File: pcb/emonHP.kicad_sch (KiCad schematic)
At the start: 66 parts, among them CN1 CONN_03SCREW, CN3 Screw_Terminal_01x02, CN4 CONN_03SCREW, CN5 Screw_Terminal_01x02, J2 CONN_04PTH, J3 USB_C_Receptacle_USB2.0, J4 Conn_ARM_JTAG_SWD_10, J5 Conn_02x20_Odd_Even, SW1 SW_Push, SW2 SW_Push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

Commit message: Manufactured board
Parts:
- removed U10: SN74LVC1T45DRL, Package_TO_SOT_SMD:SOT-563, symbol Logic_LevelTranslator:SN74LVC1T45DRL
- added C16: 100n, Capacitor_SMD:C_0402_1005Metric, symbol Device:C
- added J1: Conn_01x02, Connector_PinHeader_2.54mm:PinHeader_1x02_P2.54mm_Vertical, symbol Connector_Generic:Conn_01x02
- added R21, R24, R25, R3: 10K, Resistor_SMD:R_0402_1005Metric, symbol Device:R
- C12: LCSC (none) -> C52923
- C7: LCSC C1525 -> C23630
- D2, D3, D4: LCSC (none) -> C22440024
- FB1, FB2: LCSC (none) -> C237347
- J3: LCSC C27636760 -> C2765186
- J4: LCSC (none) -> C150517; now fitted
- LED1: LCSC (none) -> C125116
- R1: value 4K7 -> 5K1
- R11, R7: LCSC (none) -> C25744
- SW2: LCSC (none) -> C2689642
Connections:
- net +3V3: now also C16.1, R24.1; no longer D10.2 (A)
- net Boost/36V: now also J1.1 (Pin_1)
- net GND: now also C16.2, J1.2 (Pin_2), R21.2, R25.2
- net MBUS_OC: now also U2.9 (PA04)
- net RS485_RX5: now also R3.1
- net UART3_RTS: now also R25.1
- net UART3_RX: now also R21.1, R3.2
- net UART3_TX: now also R24.2
- net Vuc: now also D10.2 (A)
- net ~{LED_ACT}: now also U2.37 (PB22); no longer U2.9 (PA04)
- no-connect marks 25 -> 28
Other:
- moved on the sheet: CN5

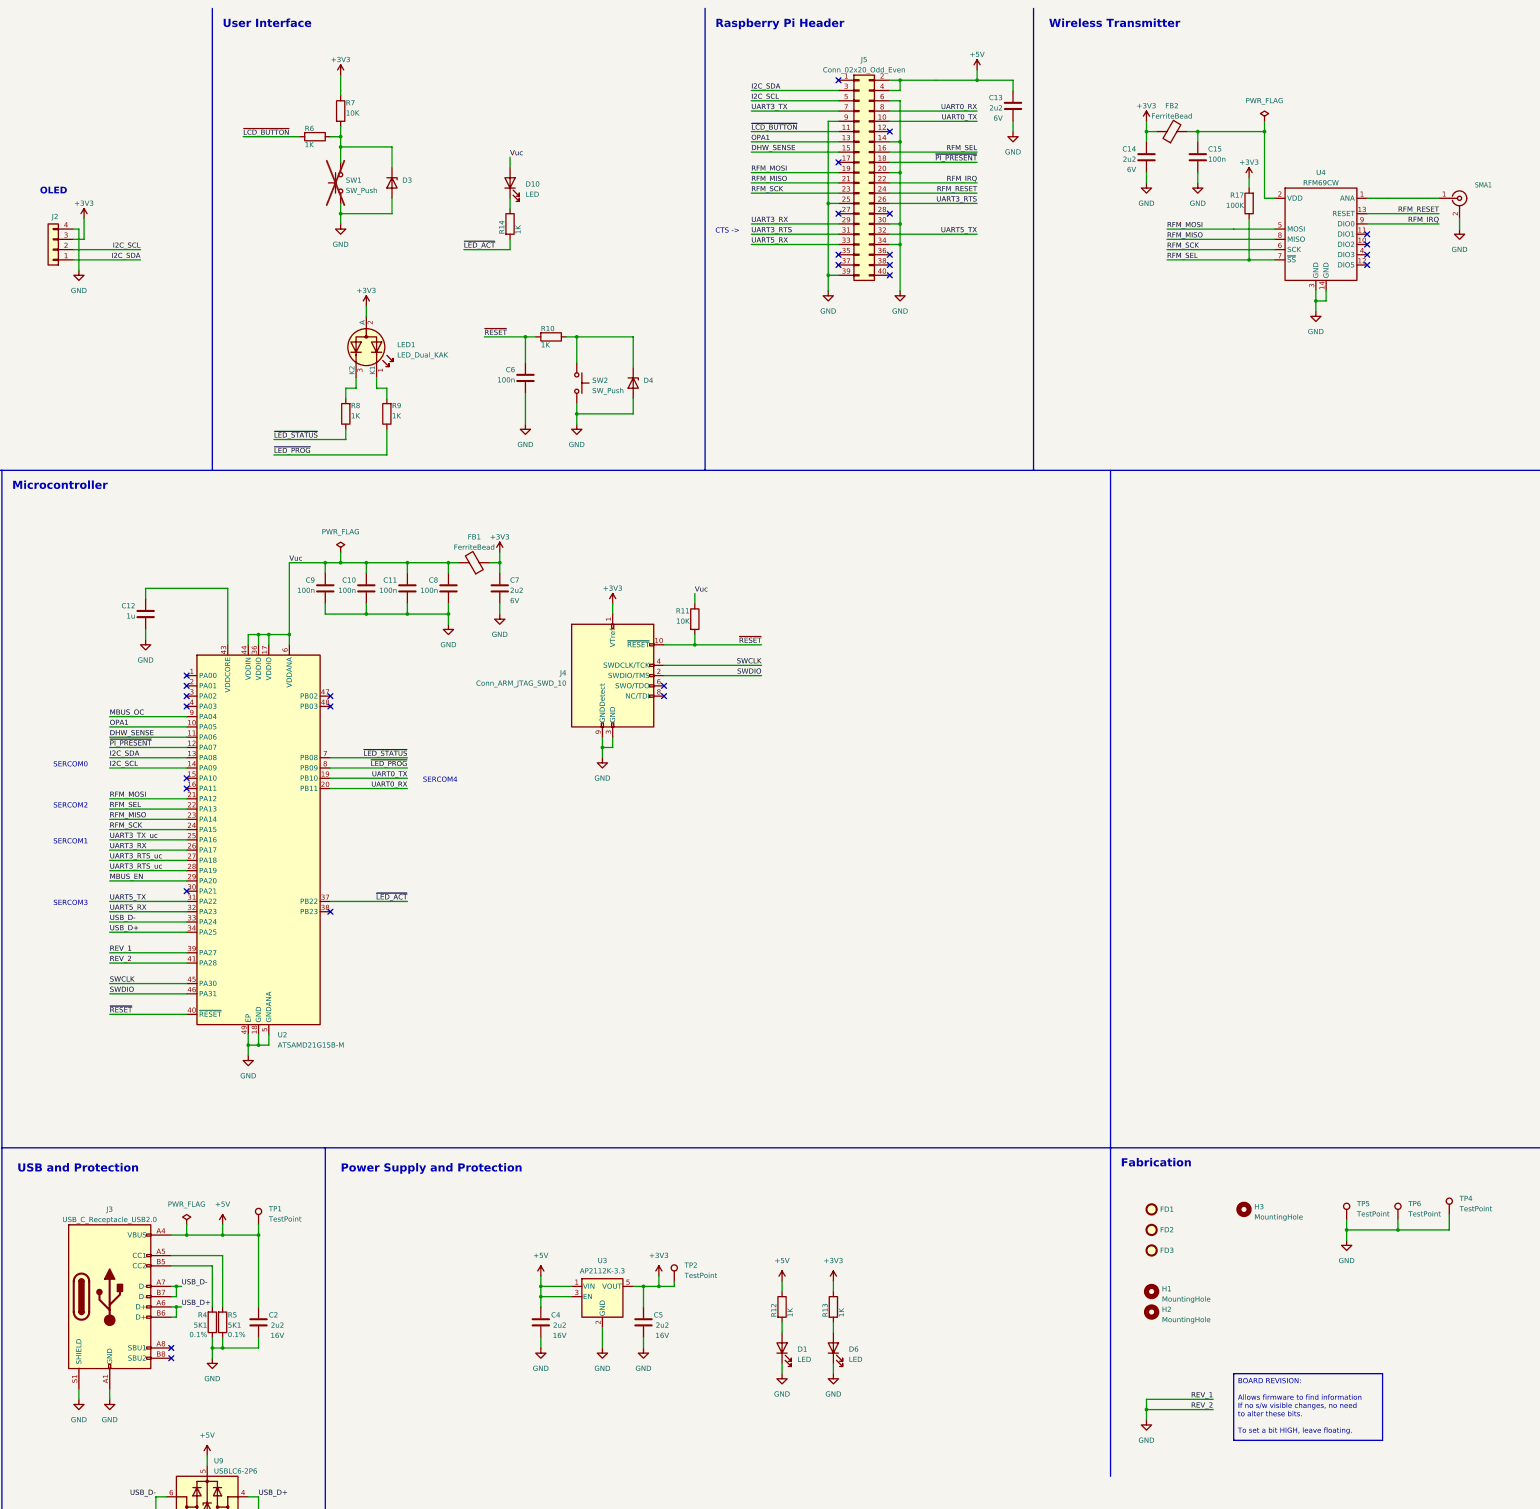
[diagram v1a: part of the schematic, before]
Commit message: emonHP with Pi attachment
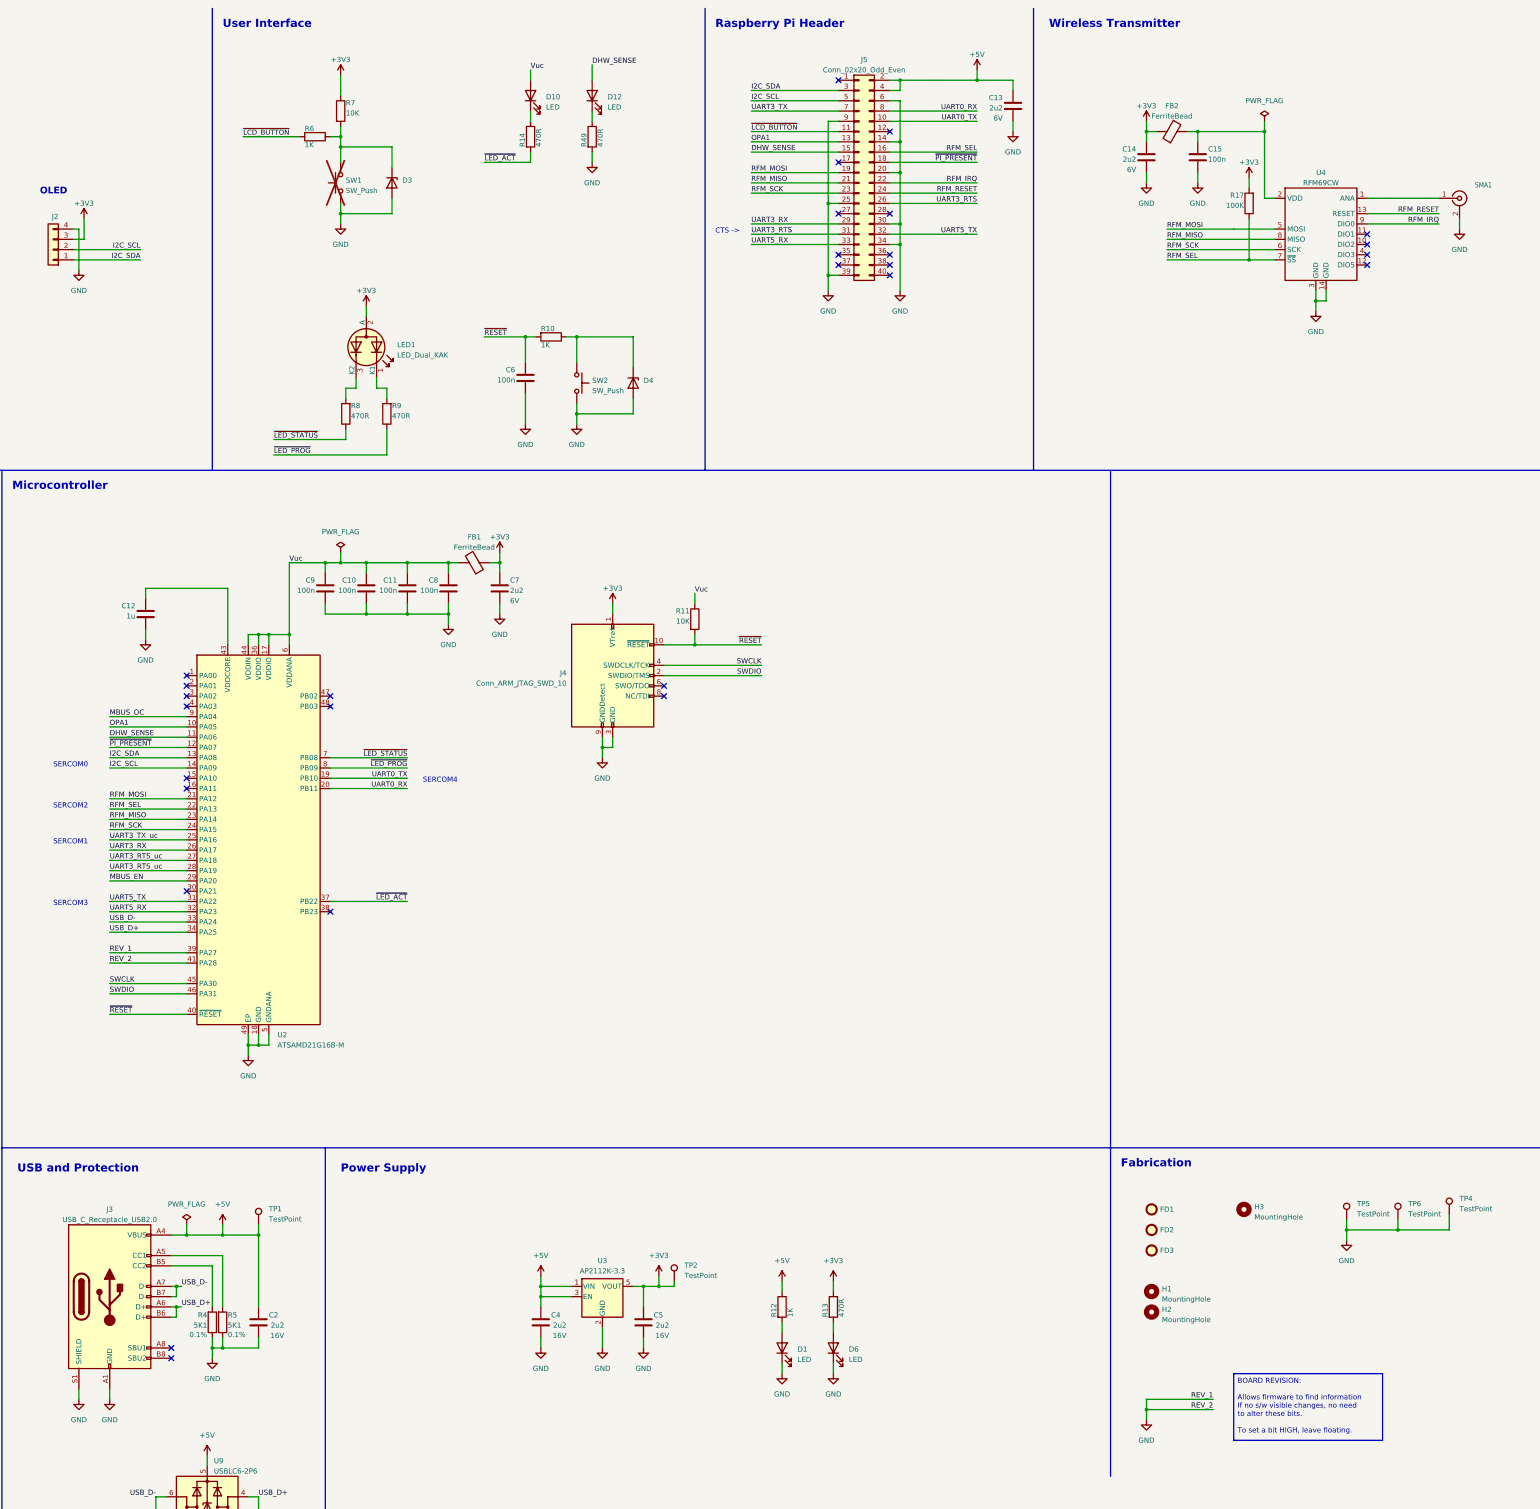
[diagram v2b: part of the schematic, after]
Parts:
- removed U2: ATSAMD21G15B-M, Package_DFN_QFN:QFN-48-1EP_7x7mm_P0.5mm_EP5.15x5.15mm, symbol MCU_Microchip_SAMD:ATSAMD21G15B-M
- added D12: LED, LED_SMD:LED_0603_1608Metric, symbol Device:LED
- added R49: 470R, Resistor_SMD:R_0402_1005Metric, symbol Device:R
- added U2: ATSAMD21G16B-M, Package_DFN_QFN:QFN-48-1EP_7x7mm_P0.5mm_EP5.15x5.15mm, symbol MCU_Microchip_SAMD:ATSAMD21G16B-M
- R13, R14, R8, R9: value 1K -> 470R; LCSC C11702 -> C25117
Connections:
- net DHW_SENSE: now also D12.2 (A), U2.11 (PA06)
- net GND: now also R49.2, U2.18 (GND), U2.35 (GND), U2.39 (PA27), U2.41 (PA28), U2.42 (GND), U2.49 (EP), U2.5 (GNDANA)
- net I2C_SCL: now also U2.14 (PA09)
- net I2C_SDA: now also U2.13 (PA08)
- net MBUS_EN: now also U2.29 (PA20)
- net MBUS_OC: now also U2.9 (PA04)
- net OPA1: now also U2.10 (PA05)
- net RFM_MISO: now also U2.23 (PA14)
- net RFM_MOSI: now also U2.21 (PA12)
- net RFM_SCK: now also U2.24 (PA15)
- net RFM_SEL: now also U2.22 (PA13)
- net SWCLK: now also U2.45 (PA30)
- net SWDIO: now also U2.46 (PA31)
- net UART0_RX: now also U2.20 (PB11)
- net UART0_TX: now also U2.19 (PB10)
- net UART3_RTS_uc: now also U2.27 (PA18), U2.28 (PA19)
- net UART3_RX: now also U2.26 (PA17)
- net UART3_TX_uc: now also U2.25 (PA16)
- net UART5_RX: now also U2.32 (PA23)
- net UART5_TX: now also U2.31 (PA22)
- net USB_D+: now also U2.34 (PA25)
- net USB_D-: now also U2.33 (PA24)
- net Vuc: now also U2.17 (VDDIO), U2.36 (VDDIO), U2.44 (VDDIN), U2.6 (VDDANA)
- net ~{LED_ACT}: now also U2.37 (PB22)
- net ~{LED_PROG}: now also U2.8 (PB09)
- net ~{LED_STATUS}: now also U2.7 (PB08)
- net ~{PI_PRESENT}: now also U2.12 (PA07)
- net ~{RESET}: now also U2.40 (~{RESET})
- net at C12.1: now also U2.43 (VDDCORE)
- new net: D12.1 (K), R49.1
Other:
- note added: "Power Supply"
- note removed: "Power Supply and Protection"
- moved on the sheet: D10, R14
